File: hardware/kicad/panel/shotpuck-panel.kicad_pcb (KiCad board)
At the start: 2 copper layers, 91 x 88.6 mm, 281 parts, among them J1_0 Samzo PR5L4015-2P-C-F, J1_1 Samzo PR5L4015-2P-C-F, J1_2 Samzo PR5L4015-2P-C-F, J1_3 Samzo PR5L4015-2P-C-F, J2_0 SWD pads, J2_1 SWD pads, J2_2 SWD pads, J2_3 SWD pads, Q1_0 DMN63D8LDW, Q1_1 DMN63D8LDW, Q1_2 DMN63D8LDW, Q1_3 DMN63D8LDW, Q2_0 DMN2004DWK, Q2_1 DMN2004DWK, Q2_2 DMN2004DWK, Q2_3 DMN2004DWK, U1_0 MDBT50Q-1MV2, U1_1 MDBT50Q-1MV2, U1_2 MDBT50Q-1MV2, U1_3 MDBT50Q-1MV2, U2_0 LSM6DSO32TR, U2_1 LSM6DSO32TR, U2_2 LSM6DSO32TR, U2_3 LSM6DSO32TR, U3_0 MCP73831T-2ACI/OT, U3_1 MCP73831T-2ACI/OT, U3_2 MCP73831T-2ACI/OT, U3_3 MCP73831T-2ACI/OT, U4_0 BQ29700DSER, U4_1 BQ29700DSER, U4_2 BQ29700DSER, U4_3 BQ29700DSER

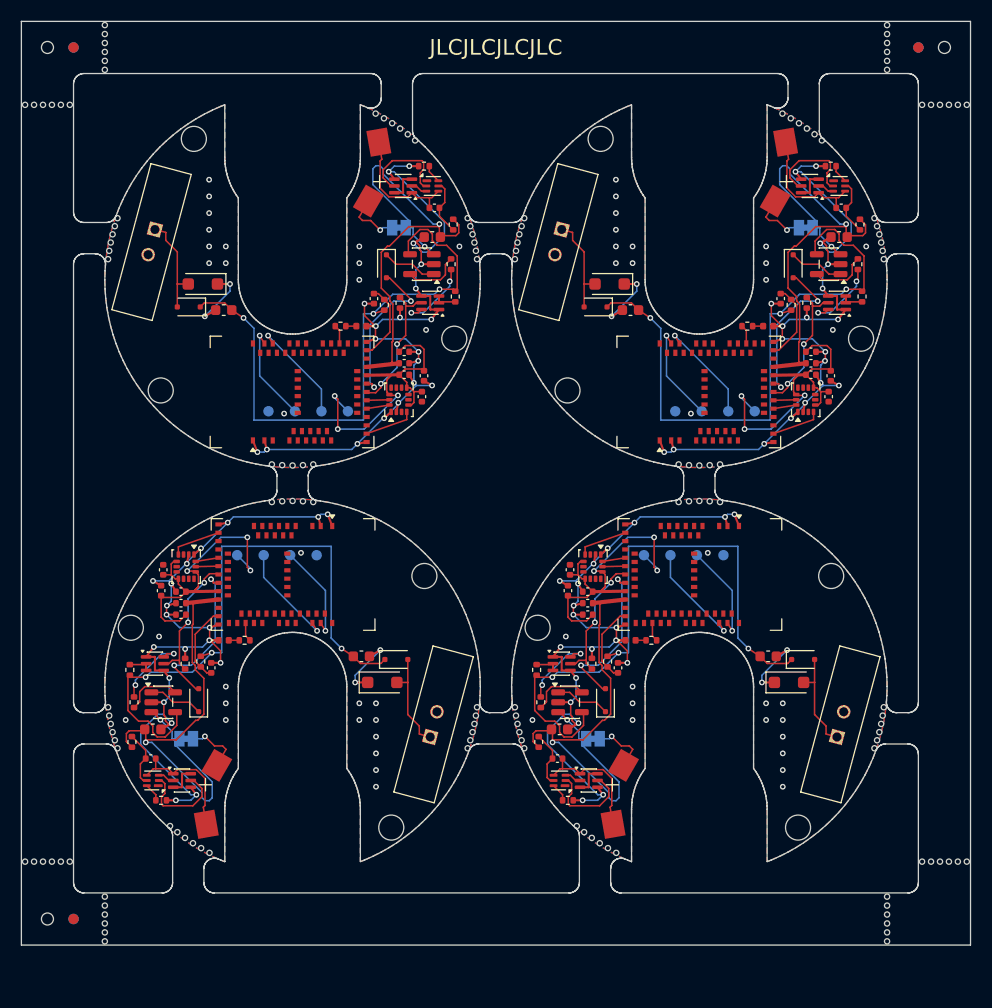
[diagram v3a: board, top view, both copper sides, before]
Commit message: Update ShotPuck design to integrate u-blox BMD-340 module and enhance documentation
- Replaced the Raytac MDBT50Q-1MV2 with the u-blox BMD-340-A-R-10 in the hardware design, updating relevant specifications in `HANDOVER.md`, `README.md`, and `VALIDATION.md`.
- Adjusted pin mappings and configurations in firmware files to reflect the new module's layout and capabilities.
- Enhanced `layout.json` and `design.py` to accommodate the new component dimensions and positions.
- Updated the bill of materials and JLCPCB configurations in `gen_bom.py` and `gen_jlc.py` to ensure accurate sourcing of the new module.
- Revised mechanical design parameters in `board_shape.py` to improve fit and stability.

Co-Authored-By: Claude Opus 5.5 <noreply@anthropic.com>
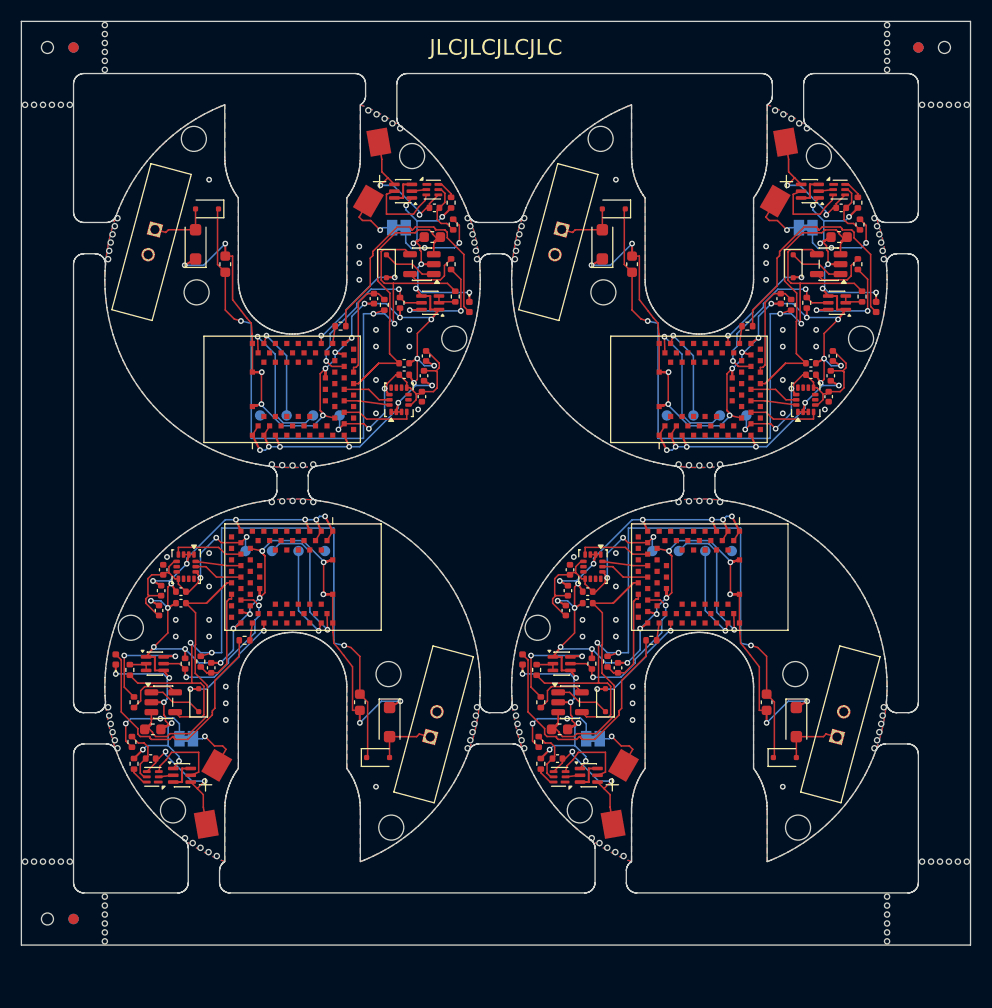
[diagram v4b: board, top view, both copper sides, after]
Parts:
- removed KiKit_MB_12_6, KiKit_MB_13_1, KiKit_MB_16_6, KiKit_MB_1_1, KiKit_MB_4_6, KiKit_MB_5_1, KiKit_MB_8_6, KiKit_MB_9_1: NPTH, NPTH
- added H4_0: M2, ShotPuck:MountingHole_2.4mm_NPTH, F.Cu at (140.5, 32.9)
- added H4_1: M2, ShotPuck:MountingHole_2.4mm_NPTH, F.Cu at (179.5, 32.9)
- added H4_2: M2, ShotPuck:MountingHole_2.4mm_NPTH, F.Cu at (117.5, 95.6)
- added H4_3: M2, ShotPuck:MountingHole_2.4mm_NPTH, F.Cu at (156.5, 95.6)
- added KiKit_MB_10_6: NPTH, NPTH, F.Cu at (145.8, 89.7)
- added KiKit_MB_14_6: NPTH, NPTH, F.Cu at (184.8, 89.7)
- added KiKit_MB_2_6: NPTH, NPTH, F.Cu at (112.2, 38.9)
- added KiKit_MB_6_6: NPTH, NPTH, F.Cu at (151.2, 38.9)
- U1_0, U1_1, U1_2, U1_3: value MDBT50Q-1MV2 -> BMD-340-A-R; footprint RF_Module:Raytac_MDBT50Q -> ShotPuck:u-blox_BMD-340
- moved KiKit_MB_14_1 27.8 mm to (185.7, 85.8)
- moved KiKit_MB_16_1 27.8 mm to (166.0, 66.1)
- moved KiKit_MB_10_1 27.8 mm to (146.7, 85.8)
- moved KiKit_MB_12_1 27.8 mm to (127.0, 66.1)
- moved KiKit_MB_6_1 27.8 mm to (150.3, 42.8)
- moved KiKit_MB_8_1 27.8 mm to (170.0, 62.5)
- moved KiKit_MB_2_1 27.8 mm to (111.3, 42.8)
- moved KiKit_MB_4_1 27.8 mm to (131.0, 62.5)
- moved KiKit_MB_14_2 27.7 mm to (185.6, 86.6)
- moved KiKit_MB_16_2 27.7 mm to (167.0, 66.0)
- moved KiKit_MB_10_2 27.7 mm to (146.6, 86.6)
- moved KiKit_MB_12_2 27.7 mm to (128.0, 66.0)
- moved KiKit_MB_6_2 27.7 mm to (150.4, 42.0)
- moved KiKit_MB_8_2 27.7 mm to (169.0, 62.5)
- moved KiKit_MB_2_2 27.7 mm to (111.4, 42.0)
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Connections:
- Q2_0 pad 1: Board_0-BAT_N -> Board_0-GND
- Q2_0 pad 2: Board_0-PCM_DOUT -> Board_0-PCM_COUT
- Q2_0 pad 4: Board_0-GND -> Board_0-BAT_N
- Q2_0 pad 5: Board_0-PCM_COUT -> Board_0-PCM_DOUT
- Q2_1 pad 1: Board_1-BAT_N -> Board_1-GND
- Q2_1 pad 2: Board_1-PCM_DOUT -> Board_1-PCM_COUT
- Q2_1 pad 4: Board_1-GND -> Board_1-BAT_N
- Q2_1 pad 5: Board_1-PCM_COUT -> Board_1-PCM_DOUT
- Q2_2 pad 1: Board_2-BAT_N -> Board_2-GND
- Q2_2 pad 2: Board_2-PCM_DOUT -> Board_2-PCM_COUT
- Q2_2 pad 4: Board_2-GND -> Board_2-BAT_N
- Q2_2 pad 5: Board_2-PCM_COUT -> Board_2-PCM_DOUT
- Q2_3 pad 1: Board_3-BAT_N -> Board_3-GND
- Q2_3 pad 2: Board_3-PCM_DOUT -> Board_3-PCM_COUT
- Q2_3 pad 4: Board_3-GND -> Board_3-BAT_N
- Q2_3 pad 5: Board_3-PCM_COUT -> Board_3-PCM_DOUT
- U1_0 pad 15: Board_0-GND -> (no net)
- U1_0 pad 16: Board_0-ACC_INT1 -> Board_0-GND
- U1_0 pad 17: (no net) -> Board_0-VDD
- U1_0 pad 18: (no net) -> Board_0-GND
- U1_0 pad 19: (no net) -> Board_0-ACC_INT1
- U1_0 pad 20: Board_0-SDA -> (no net)
- U1_0 pad 21: (no net) -> Board_0-SDA
- U1_0 pad 22: Board_0-SCL -> (no net)
- U1_0 pad 23: (no net) -> Board_0-SCL
- U1_0 pad 24: Board_0-CHG_INH -> (no net)
- U1_0 pad 26: Board_0-CHG_STAT -> (no net)
- U1_0 pad 27: (no net) -> Board_0-CHG_INH
- U1_0 pad 28: Board_0-VDD -> (no net)
- U1_0 pad 29: (no net) -> Board_0-GND
- U1_0 pad 3: (no net) -> Board_0-GND
- U1_0 pad 30: Board_0-VBAT -> Board_0-GND
- U1_0 pad 31: (no net) -> Board_0-LED_IO
- U1_0 pad 32: Board_0-VBUS_SNS -> (no net)
- U1_0 pad 33: Board_0-GND -> Board_0-CHG_STAT
- U1_0 pad 37: Board_0-LED_IO -> (no net)
- U1_0 pad 4: (no net) -> Board_0-GND
- U1_0 pad 43: (no net) -> Board_0-SWDCLK
- U1_0 pad 44: (no net) -> Board_0-SWDIO
- U1_0 pad 45: (no net) -> Board_0-GND
- U1_0 pad 46: (no net) -> Board_0-GND
- U1_0 pad 47: (no net) -> Board_0-GND
- U1_0 pad 5: (no net) -> Board_0-GND
- U1_0 pad 51: Board_0-SWDIO -> (no net)
- U1_0 pad 53: Board_0-SWDCLK -> (no net)
- U1_1 pad 15: Board_1-GND -> (no net)
- U1_1 pad 16: Board_1-ACC_INT1 -> Board_1-GND
- U1_1 pad 17: (no net) -> Board_1-VDD
- U1_1 pad 18: (no net) -> Board_1-GND
- U1_1 pad 19: (no net) -> Board_1-ACC_INT1
- U1_1 pad 20: Board_1-SDA -> (no net)
- U1_1 pad 21: (no net) -> Board_1-SDA
- U1_1 pad 22: Board_1-SCL -> (no net)
- U1_1 pad 23: (no net) -> Board_1-SCL
- U1_1 pad 24: Board_1-CHG_INH -> (no net)
- U1_1 pad 26: Board_1-CHG_STAT -> (no net)
- U1_1 pad 27: (no net) -> Board_1-CHG_INH
- U1_1 pad 28: Board_1-VDD -> (no net)
- U1_1 pad 29: (no net) -> Board_1-GND
- U1_1 pad 3: (no net) -> Board_1-GND
- U1_1 pad 30: Board_1-VBAT -> Board_1-GND
- U1_1 pad 31: (no net) -> Board_1-LED_IO
- U1_1 pad 32: Board_1-VBUS_SNS -> (no net)
- U1_1 pad 33: Board_1-GND -> Board_1-CHG_STAT
- U1_1 pad 37: Board_1-LED_IO -> (no net)
- U1_1 pad 4: (no net) -> Board_1-GND
- U1_1 pad 43: (no net) -> Board_1-SWDCLK
- U1_1 pad 44: (no net) -> Board_1-SWDIO
- U1_1 pad 45: (no net) -> Board_1-GND
- U1_1 pad 46: (no net) -> Board_1-GND
- U1_1 pad 47: (no net) -> Board_1-GND
- U1_1 pad 5: (no net) -> Board_1-GND
- U1_1 pad 51: Board_1-SWDIO -> (no net)
- U1_1 pad 53: Board_1-SWDCLK -> (no net)
- U1_2 pad 15: Board_2-GND -> (no net)
- U1_2 pad 16: Board_2-ACC_INT1 -> Board_2-GND
- U1_2 pad 17: (no net) -> Board_2-VDD
- U1_2 pad 18: (no net) -> Board_2-GND
- U1_2 pad 19: (no net) -> Board_2-ACC_INT1
- U1_2 pad 20: Board_2-SDA -> (no net)
- U1_2 pad 21: (no net) -> Board_2-SDA
- U1_2 pad 22: Board_2-SCL -> (no net)
- U1_2 pad 23: (no net) -> Board_2-SCL
- U1_2 pad 24: Board_2-CHG_INH -> (no net)
- U1_2 pad 26: Board_2-CHG_STAT -> (no net)
- U1_2 pad 27: (no net) -> Board_2-CHG_INH
- U1_2 pad 28: Board_2-VDD -> (no net)
- U1_2 pad 29: (no net) -> Board_2-GND
- U1_2 pad 3: (no net) -> Board_2-GND
- U1_2 pad 30: Board_2-VBAT -> Board_2-GND
- U1_2 pad 31: (no net) -> Board_2-LED_IO
- U1_2 pad 32: Board_2-VBUS_SNS -> (no net)
- U1_2 pad 33: Board_2-GND -> Board_2-CHG_STAT
- U1_2 pad 37: Board_2-LED_IO -> (no net)
- U1_2 pad 4: (no net) -> Board_2-GND
- U1_2 pad 43: (no net) -> Board_2-SWDCLK
- U1_2 pad 44: (no net) -> Board_2-SWDIO
- U1_2 pad 45: (no net) -> Board_2-GND
- U1_2 pad 46: (no net) -> Board_2-GND
- U1_2 pad 47: (no net) -> Board_2-GND
- U1_2 pad 5: (no net) -> Board_2-GND
- U1_2 pad 51: Board_2-SWDIO -> (no net)
- U1_2 pad 53: Board_2-SWDCLK -> (no net)
- U1_3 pad 15: Board_3-GND -> (no net)
- U1_3 pad 16: Board_3-ACC_INT1 -> Board_3-GND
- U1_3 pad 17: (no net) -> Board_3-VDD
- U1_3 pad 18: (no net) -> Board_3-GND
- U1_3 pad 19: (no net) -> Board_3-ACC_INT1
- U1_3 pad 20: Board_3-SDA -> (no net)
- U1_3 pad 21: (no net) -> Board_3-SDA
- U1_3 pad 22: Board_3-SCL -> (no net)
- U1_3 pad 23: (no net) -> Board_3-SCL
- U1_3 pad 24: Board_3-CHG_INH -> (no net)
- U1_3 pad 26: Board_3-CHG_STAT -> (no net)
- U1_3 pad 27: (no net) -> Board_3-CHG_INH
- U1_3 pad 28: Board_3-VDD -> (no net)
- U1_3 pad 29: (no net) -> Board_3-GND
- U1_3 pad 3: (no net) -> Board_3-GND
- U1_3 pad 30: Board_3-VBAT -> Board_3-GND
- U1_3 pad 31: (no net) -> Board_3-LED_IO
- U1_3 pad 32: Board_3-VBUS_SNS -> (no net)
- U1_3 pad 33: Board_3-GND -> Board_3-CHG_STAT
- U1_3 pad 37: Board_3-LED_IO -> (no net)
- U1_3 pad 4: (no net) -> Board_3-GND
- U1_3 pad 43: (no net) -> Board_3-SWDCLK
- U1_3 pad 44: (no net) -> Board_3-SWDIO
- U1_3 pad 45: (no net) -> Board_3-GND
- U1_3 pad 46: (no net) -> Board_3-GND
- U1_3 pad 47: (no net) -> Board_3-GND
- U1_3 pad 5: (no net) -> Board_3-GND
- U1_3 pad 51: Board_3-SWDIO -> (no net)
- U1_3 pad 53: Board_3-SWDCLK -> (no net)
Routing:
- net Board_3-GND: track 86.8 -> 131.6 mm, vias 35 -> 37
- net Board_2-GND: track 86.8 -> 131.6 mm, vias 35 -> 37
- net Board_1-GND: track 86.8 -> 131.6 mm, vias 35 -> 37
- net Board_0-GND: track 86.8 -> 131.6 mm, vias 35 -> 37
- net Board_2-LED_A: track 1.00 -> 25.4 mm
- net Board_3-LED_A: track 1.00 -> 25.4 mm
- net Board_1-LED_A: track 1.00 -> 25.4 mm
- net Board_0-LED_A: track 1.00 -> 25.4 mm
- net Board_0-VIN: track 58.1 -> 68.4 mm
- net Board_3-VIN: track 58.1 -> 68.4 mm
- net Board_1-VIN: track 58.1 -> 68.4 mm
- net Board_2-VIN: track 58.1 -> 68.4 mm
- net Board_2-PCM_COUT: track 9.30 -> 1.40 mm
- net Board_3-PCM_COUT: track 9.30 -> 1.40 mm
- net Board_1-PCM_COUT: track 9.30 -> 1.40 mm
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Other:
- outline, holes or cut-outs redrawn

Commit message: Switch J1 to waterproof IPX8 USB-C (C3020041) and seal the cap
- J1: SHOU HAN TYPE-C 6PFS 2JCB1.6-H6.7 IPX8 (LCSC C3020041), recessed
  into a 10.28 x 5.22 mm notch in the board edge at 132.58 deg, midway
  between H1 and H2. Footprint from the datasheet drawing (pads kept
  0.3/0.35 mm from the notch; the notch sides run through two 0.70 mm
  NPTH holes for the legs, since the datasheet's 0.69 mm U-slots cannot
  be routed); LCSC's STEP model shifted -1.93 mm onto the pads.
- H1/H2 moved apart so the ground pour reaches the wing tabs; layout.json
  bosses follow (plate holes, cap bosses, standoffs).
- GND via at (-0.41, 16.09): the pour around U2's GND pins 6/7 reached
  the rest of GND only along the rim, where the top tab's mouse bites cut
  it.
- Cap: the silicone ring seals in an obround hole in the wall (0.15 mm
  squeeze per side), a flat at the receptacle face lets any compliant
  plug seat fully, a pocket over the body leaves 0.67 mm of cap top.
  CadQuery check with the real STEP model: only the ring squeeze
  overlaps; a maximum-size plug overmold clears cap and plate.
- Panel: 2 mm backbone between the rows, top tab 1.5 mm wide at 86 deg
  (clear of H1 and the via at 80 deg); panel 91.1 x 92.7 mm.
- gen_panel.py places tabs from the board's own centre (the board sits at
  (132.06, 91.40) on the KiCad page); the Blender GLB export uses the
  same origin and takes J1 from the board.
- Board DRC 0/0 with schematic parity; panel DRC 0/0; BOM/CPL/Gerbers
  regenerated.

mechanical/out/shotpuck_assembly.mp4 and .blend are from the render
before the waterproof port and still show the earlier cap; re-render
with mechanical/blender/render_assembly.py. gen_pcb.py does not draw
the port notch, and design.py still lists C5.

Co-Authored-By: Claude Opus 5.5 <noreply@anthropic.com>
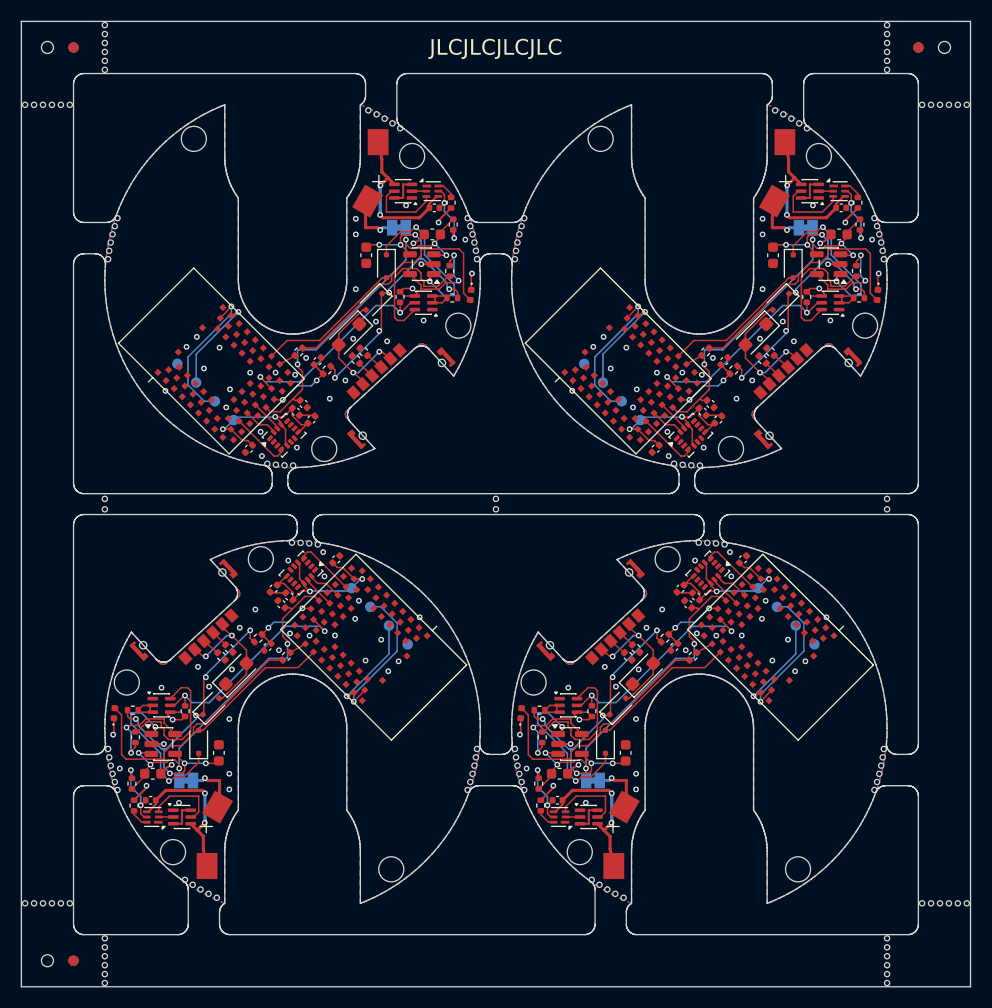
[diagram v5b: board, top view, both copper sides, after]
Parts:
- removed C5_0, C5_1, C5_2, C5_3: 100n, Capacitor_SMD:C_0402_1005Metric
- removed KiKit_MB_10_5, KiKit_MB_10_6, KiKit_MB_11_1, KiKit_MB_14_5, KiKit_MB_14_6, KiKit_MB_15_1, KiKit_MB_17_4, KiKit_MB_17_5, KiKit_MB_17_6, KiKit_MB_17_7, KiKit_MB_18_4, KiKit_MB_18_5, KiKit_MB_18_6, KiKit_MB_18_7, KiKit_MB_19_4, KiKit_MB_19_5, KiKit_MB_19_6, KiKit_MB_19_7, KiKit_MB_2_5, KiKit_MB_2_6, KiKit_MB_3_1, KiKit_MB_6_5, KiKit_MB_6_6, KiKit_MB_7_1: NPTH, NPTH
- added KiKit_MB_12_6: NPTH, NPTH, F.Cu at (111.3, 89.8)
- added KiKit_MB_13_1: NPTH, NPTH, F.Cu at (185.7, 89.8)
- added KiKit_MB_16_6: NPTH, NPTH, F.Cu at (150.3, 89.8)
- added KiKit_MB_1_1: NPTH, NPTH, F.Cu at (111.3, 42.8)
- added KiKit_MB_25_2: NPTH, NPTH, F.Cu at (103.4, 104.6)
- added KiKit_MB_25_3: NPTH, NPTH, F.Cu at (104.2, 104.6)
- added KiKit_MB_25_4: NPTH, NPTH, F.Cu at (105.1, 104.6)
- added KiKit_MB_25_5: NPTH, NPTH, F.Cu at (105.9, 104.6)
- added KiKit_MB_25_6: NPTH, NPTH, F.Cu at (106.8, 104.6)
- added KiKit_MB_25_7: NPTH, NPTH, F.Cu at (107.6, 104.6)
- added KiKit_MB_26_2: NPTH, NPTH, F.Cu at (189.4, 28.0)
- added KiKit_MB_26_3: NPTH, NPTH, F.Cu at (190.2, 28.0)
- added KiKit_MB_26_4: NPTH, NPTH, F.Cu at (191.1, 28.0)
- added KiKit_MB_26_5: NPTH, NPTH, F.Cu at (191.9, 28.0)
- added KiKit_MB_26_6: NPTH, NPTH, F.Cu at (192.8, 28.0)
- added KiKit_MB_26_7: NPTH, NPTH, F.Cu at (193.6, 28.0)
- added KiKit_MB_27_2: NPTH, NPTH, F.Cu at (189.4, 104.6)
- added KiKit_MB_27_3: NPTH, NPTH, F.Cu at (190.2, 104.6)
- added KiKit_MB_27_4: NPTH, NPTH, F.Cu at (191.1, 104.6)
- added KiKit_MB_27_5: NPTH, NPTH, F.Cu at (191.9, 104.6)
- added KiKit_MB_27_6: NPTH, NPTH, F.Cu at (192.8, 104.6)
- added KiKit_MB_27_7: NPTH, NPTH, F.Cu at (193.6, 104.6)
- added KiKit_MB_4_6: NPTH, NPTH, F.Cu at (146.7, 42.8)
- added KiKit_MB_5_1: NPTH, NPTH, F.Cu at (150.3, 42.8)
- added KiKit_MB_8_6: NPTH, NPTH, F.Cu at (185.7, 42.8)
- added KiKit_MB_9_1: NPTH, NPTH, F.Cu at (146.7, 89.8)
- added R10_0: 5.1k 1%, Resistor_SMD:R_0402_1005Metric, F.Cu at (135.1, 52.4)
- added R10_1: 5.1k 1%, Resistor_SMD:R_0402_1005Metric, F.Cu at (174.1, 52.4)
- added R10_2: 5.1k 1%, Resistor_SMD:R_0402_1005Metric, F.Cu at (122.9, 80.1)
- added R10_3: 5.1k 1%, Resistor_SMD:R_0402_1005Metric, F.Cu at (161.9, 80.1)
- added R11_0: 5.1k 1%, Resistor_SMD:R_0402_1005Metric, F.Cu at (135.8, 51.7)
- added R11_1: 5.1k 1%, Resistor_SMD:R_0402_1005Metric, F.Cu at (174.8, 51.7)
- added R11_2: 5.1k 1%, Resistor_SMD:R_0402_1005Metric, F.Cu at (122.2, 80.9)
- added R11_3: 5.1k 1%, Resistor_SMD:R_0402_1005Metric, F.Cu at (161.2, 80.9)
- BT1_0, BT1_1, BT1_2, BT1_3: footprint ShotPuck:LIR1254_Contacts -> ShotPuck:LIR1254_Contacts_Edit
- J1_0, J1_1, J1_2, J1_3: value Samzo PR5L4015-2P-C-F -> TYPE-C 6PFS 2JCB1.6-H6.7 IPX8; footprint ShotPuck:MagPogo_Samzo_2P -> ShotPuck:USB_C_Receptacle_ShouHan_TYPE-C-6PFS-2JCB1.6-H6.7_IPX8
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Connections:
- net Board_0-ACC_INT1 renamed Board_0-/ACC_INT1
- net Board_0-BAT_N renamed Board_0-/BAT_N
- net Board_0-BAT_P renamed Board_0-/BAT_P
- net Board_0-CHG_INH renamed Board_0-/CHG_INH
- net Board_0-CHG_STAT renamed Board_0-/CHG_STAT
- net Board_0-LED_A renamed Board_0-/LED_A
- net Board_0-LED_IO renamed Board_0-/LED_IO
- net Board_0-PCM_BAT renamed Board_0-/PCM_BAT
- net Board_0-PCM_COUT renamed Board_0-/PCM_COUT
- net Board_0-PCM_D renamed Board_0-/PCM_D
- net Board_0-PCM_DOUT renamed Board_0-/PCM_DOUT
- net Board_0-PCM_VM renamed Board_0-/PCM_VM
- net Board_0-PROG renamed Board_0-/PROG
- net Board_0-PROG_SW renamed Board_0-/PROG_SW
- net Board_0-Q1_GATE renamed Board_0-/Q1_GATE
- net Board_0-SCL renamed Board_0-/SCL
- net Board_0-SDA renamed Board_0-/SDA
- net Board_0-STAT renamed Board_0-/STAT
- net Board_0-SWDCLK renamed Board_0-/SWDCLK
- net Board_0-SWDIO renamed Board_0-/SWDIO
- net Board_0-VBAT renamed Board_0-/VBAT
- net Board_0-VBUS_SNS renamed Board_0-/VBUS_SNS
- net Board_0-VDD renamed Board_0-/VDD
- net Board_0-VIN renamed Board_0-/VIN
- net Board_1-ACC_INT1 renamed Board_1-/ACC_INT1
- net Board_1-BAT_N renamed Board_1-/BAT_N
- net Board_1-BAT_P renamed Board_1-/BAT_P
- net Board_1-CHG_INH renamed Board_1-/CHG_INH
- net Board_1-CHG_STAT renamed Board_1-/CHG_STAT
- net Board_1-LED_A renamed Board_1-/LED_A
- net Board_1-LED_IO renamed Board_1-/LED_IO
- net Board_1-PCM_BAT renamed Board_1-/PCM_BAT
- net Board_1-PCM_COUT renamed Board_1-/PCM_COUT
- net Board_1-PCM_D renamed Board_1-/PCM_D
- net Board_1-PCM_DOUT renamed Board_1-/PCM_DOUT
- net Board_1-PCM_VM renamed Board_1-/PCM_VM
- net Board_1-PROG renamed Board_1-/PROG
- net Board_1-PROG_SW renamed Board_1-/PROG_SW
- net Board_1-Q1_GATE renamed Board_1-/Q1_GATE
- net Board_1-SCL renamed Board_1-/SCL
- net Board_1-SDA renamed Board_1-/SDA
- net Board_1-STAT renamed Board_1-/STAT
- net Board_1-SWDCLK renamed Board_1-/SWDCLK
- net Board_1-SWDIO renamed Board_1-/SWDIO
- net Board_1-VBAT renamed Board_1-/VBAT
- net Board_1-VBUS_SNS renamed Board_1-/VBUS_SNS
- net Board_1-VDD renamed Board_1-/VDD
- net Board_1-VIN renamed Board_1-/VIN
- net Board_2-ACC_INT1 renamed Board_2-/ACC_INT1
- net Board_2-BAT_N renamed Board_2-/BAT_N
- net Board_2-BAT_P renamed Board_2-/BAT_P
- net Board_2-CHG_INH renamed Board_2-/CHG_INH
- net Board_2-CHG_STAT renamed Board_2-/CHG_STAT
- net Board_2-LED_A renamed Board_2-/LED_A
- net Board_2-LED_IO renamed Board_2-/LED_IO
- net Board_2-PCM_BAT renamed Board_2-/PCM_BAT
- net Board_2-PCM_COUT renamed Board_2-/PCM_COUT
- net Board_2-PCM_D renamed Board_2-/PCM_D
- net Board_2-PCM_DOUT renamed Board_2-/PCM_DOUT
- net Board_2-PCM_VM renamed Board_2-/PCM_VM
- net Board_2-PROG renamed Board_2-/PROG
- net Board_2-PROG_SW renamed Board_2-/PROG_SW
- net Board_2-Q1_GATE renamed Board_2-/Q1_GATE
- net Board_2-SCL renamed Board_2-/SCL
- net Board_2-SDA renamed Board_2-/SDA
- net Board_2-STAT renamed Board_2-/STAT
- net Board_2-SWDCLK renamed Board_2-/SWDCLK
- net Board_2-SWDIO renamed Board_2-/SWDIO
- net Board_2-VBAT renamed Board_2-/VBAT
- net Board_2-VBUS_SNS renamed Board_2-/VBUS_SNS
- net Board_2-VDD renamed Board_2-/VDD
- net Board_2-VIN renamed Board_2-/VIN
- net Board_3-ACC_INT1 renamed Board_3-/ACC_INT1
- net Board_3-BAT_N renamed Board_3-/BAT_N
- net Board_3-BAT_P renamed Board_3-/BAT_P
- net Board_3-CHG_INH renamed Board_3-/CHG_INH
- net Board_3-CHG_STAT renamed Board_3-/CHG_STAT
- net Board_3-LED_A renamed Board_3-/LED_A
- net Board_3-LED_IO renamed Board_3-/LED_IO
- net Board_3-PCM_BAT renamed Board_3-/PCM_BAT
- net Board_3-PCM_COUT renamed Board_3-/PCM_COUT
- net Board_3-PCM_D renamed Board_3-/PCM_D
- net Board_3-PCM_DOUT renamed Board_3-/PCM_DOUT
- net Board_3-PCM_VM renamed Board_3-/PCM_VM
- net Board_3-PROG renamed Board_3-/PROG
- net Board_3-PROG_SW renamed Board_3-/PROG_SW
- net Board_3-Q1_GATE renamed Board_3-/Q1_GATE
- net Board_3-SCL renamed Board_3-/SCL
- net Board_3-SDA renamed Board_3-/SDA
- net Board_3-STAT renamed Board_3-/STAT
- net Board_3-SWDCLK renamed Board_3-/SWDCLK
- net Board_3-SWDIO renamed Board_3-/SWDIO
- net Board_3-VBAT renamed Board_3-/VBAT
- net Board_3-VBUS_SNS renamed Board_3-/VBUS_SNS
- net Board_3-VDD renamed Board_3-/VDD
- net Board_3-VIN renamed Board_3-/VIN
- C1_0 pad 2: Board_0-GND -> Board_0-/GND
- C1_1 pad 2: Board_1-GND -> Board_1-/GND
- C1_2 pad 2: Board_2-GND -> Board_2-/GND
- C1_3 pad 2: Board_3-GND -> Board_3-/GND
- C2_0 pad 2: Board_0-GND -> Board_0-/GND
- C2_1 pad 2: Board_1-GND -> Board_1-/GND
- C2_2 pad 2: Board_2-GND -> Board_2-/GND
- C2_3 pad 2: Board_3-GND -> Board_3-/GND
- C3_0 pad 2: Board_0-GND -> Board_0-/GND
- C3_1 pad 2: Board_1-GND -> Board_1-/GND
- C3_2 pad 2: Board_2-GND -> Board_2-/GND
- C3_3 pad 2: Board_3-GND -> Board_3-/GND
- C4_0 pad 2: Board_0-GND -> Board_0-/GND
- C4_1 pad 2: Board_1-GND -> Board_1-/GND
- C4_2 pad 2: Board_2-GND -> Board_2-/GND
- C4_3 pad 2: Board_3-GND -> Board_3-/GND
- C6_0 pad 2: Board_0-GND -> Board_0-/GND
- C6_1 pad 2: Board_1-GND -> Board_1-/GND
- C6_2 pad 2: Board_2-GND -> Board_2-/GND
- C6_3 pad 2: Board_3-GND -> Board_3-/GND
- C7_0 pad 2: Board_0-GND -> Board_0-/GND
- C7_1 pad 2: Board_1-GND -> Board_1-/GND
- C7_2 pad 2: Board_2-GND -> Board_2-/GND
- C7_3 pad 2: Board_3-GND -> Board_3-/GND
- C9_0 pad 2: Board_0-GND -> Board_0-/GND
- C9_1 pad 2: Board_1-GND -> Board_1-/GND
- C9_2 pad 2: Board_2-GND -> Board_2-/GND
- C9_3 pad 2: Board_3-GND -> Board_3-/GND
- D1_0 pad 2: Board_0-VIN_RAW -> Board_0-/VIN_RAW
- D1_1 pad 2: Board_1-VIN_RAW -> Board_1-/VIN_RAW
- D1_2 pad 2: Board_2-VIN_RAW -> Board_2-/VIN_RAW
- D1_3 pad 2: Board_3-VIN_RAW -> Board_3-/VIN_RAW
- D3_0 pad 1: Board_0-GND -> Board_0-/GND
- D3_0 pad 2: Board_0-VIN_RAW -> Board_0-/VIN_RAW
- D3_1 pad 1: Board_1-GND -> Board_1-/GND
- D3_1 pad 2: Board_1-VIN_RAW -> Board_1-/VIN_RAW
- D3_2 pad 1: Board_2-GND -> Board_2-/GND
- D3_2 pad 2: Board_2-VIN_RAW -> Board_2-/VIN_RAW
- D3_3 pad 1: Board_3-GND -> Board_3-/GND
- D3_3 pad 2: Board_3-VIN_RAW -> Board_3-/VIN_RAW
- D4_0 pad 1: Board_0-GND -> Board_0-/GND
- D4_1 pad 1: Board_1-GND -> Board_1-/GND
- D4_2 pad 1: Board_2-GND -> Board_2-/GND
- D4_3 pad 1: Board_3-GND -> Board_3-/GND
- J2_0 pad 4: Board_0-GND -> Board_0-/GND
- J2_1 pad 4: Board_1-GND -> Board_1-/GND
- J2_2 pad 4: Board_2-GND -> Board_2-/GND
- J2_3 pad 4: Board_3-GND -> Board_3-/GND
- Q1_0 pad 1: Board_0-GND -> Board_0-/GND
- Q1_0 pad 4: Board_0-GND -> Board_0-/GND
- Q1_1 pad 1: Board_1-GND -> Board_1-/GND
- Q1_1 pad 4: Board_1-GND -> Board_1-/GND
- Q1_2 pad 1: Board_2-GND -> Board_2-/GND
- Q1_2 pad 4: Board_2-GND -> Board_2-/GND
- Q1_3 pad 1: Board_3-GND -> Board_3-/GND
- Q1_3 pad 4: Board_3-GND -> Board_3-/GND
- Q2_0 pad 1: Board_0-GND -> Board_0-/GND
- Q2_1 pad 1: Board_1-GND -> Board_1-/GND
- Q2_2 pad 1: Board_2-GND -> Board_2-/GND
- Q2_3 pad 1: Board_3-GND -> Board_3-/GND
- R3_0 pad 2: Board_0-GND -> Board_0-/GND
- R3_1 pad 2: Board_1-GND -> Board_1-/GND
- R3_2 pad 2: Board_2-GND -> Board_2-/GND
- R3_3 pad 2: Board_3-GND -> Board_3-/GND
- R8_0 pad 2: Board_0-GND -> Board_0-/GND
- R8_1 pad 2: Board_1-GND -> Board_1-/GND
- R8_2 pad 2: Board_2-GND -> Board_2-/GND
- R8_3 pad 2: Board_3-GND -> Board_3-/GND
- U1_0 pad 1: Board_0-GND -> Board_0-/GND
- U1_0 pad 10: (no net) -> Board_0-unconnected-(U1-P0.29-Pad10)
- U1_0 pad 11: (no net) -> Board_0-unconnected-(U1-P0.30-Pad11)
- U1_0 pad 12: (no net) -> Board_0-unconnected-(U1-P0.31-Pad12)
- U1_0 pad 13: (no net) -> Board_0-unconnected-(U1-P0.00-Pad13)
- U1_0 pad 14: (no net) -> Board_0-unconnected-(U1-P0.01-Pad14)
- U1_0 pad 15: (no net) -> Board_0-unconnected-(U1-P0.02-Pad15)
- U1_0 pad 16: Board_0-GND -> Board_0-/GND
- U1_0 pad 18: Board_0-GND -> Board_0-/GND
- U1_0 pad 2: Board_0-GND -> Board_0-/GND
- U1_0 pad 20: (no net) -> Board_0-unconnected-(U1-P0.04-Pad20)
- U1_0 pad 22: (no net) -> Board_0-unconnected-(U1-P0.06-Pad22)
- U1_0 pad 24: (no net) -> Board_0-unconnected-(U1-P0.08-Pad24)
- U1_0 pad 25: (no net) -> Board_0-unconnected-(U1-P0.09-Pad25)
- U1_0 pad 26: (no net) -> Board_0-unconnected-(U1-P0.10-Pad26)
- U1_0 pad 28: (no net) -> Board_0-unconnected-(U1-P0.12-Pad28)
- U1_0 pad 29: Board_0-GND -> Board_0-/GND
- U1_0 pad 3: Board_0-GND -> Board_0-/GND
- U1_0 pad 30: Board_0-GND -> Board_0-/GND
- U1_0 pad 32: (no net) -> Board_0-unconnected-(U1-P0.14-Pad32)
- U1_0 pad 34: (no net) -> Board_0-unconnected-(U1-P0.16-Pad34)
- U1_0 pad 35: (no net) -> Board_0-unconnected-(U1-P0.17-Pad35)
- U1_0 pad 36: (no net) -> Board_0-unconnected-(U1-P0.21-Pad36)
- U1_0 pad 37: (no net) -> Board_0-unconnected-(U1-P0.19-Pad37)
- U1_0 pad 38: (no net) -> Board_0-unconnected-(U1-P0.20-Pad38)
- U1_0 pad 39: (no net) -> Board_0-unconnected-(U1-P0.18-Pad39)
- U1_0 pad 4: Board_0-GND -> Board_0-/GND
- U1_0 pad 40: (no net) -> Board_0-unconnected-(U1-P0.22-Pad40)
- U1_0 pad 41: (no net) -> Board_0-unconnected-(U1-P0.23-Pad41)
- U1_0 pad 42: (no net) -> Board_0-unconnected-(U1-P0.24-Pad42)
- U1_0 pad 45: Board_0-GND -> Board_0-/GND
- U1_0 pad 46: Board_0-GND -> Board_0-/GND
- U1_0 pad 47: Board_0-GND -> Board_0-/GND
- U1_0 pad 48: (no net) -> Board_0-unconnected-(U1-P1.05-Pad48)
- U1_0 pad 49: (no net) -> Board_0-unconnected-(U1-P1.06-Pad49)
- U1_0 pad 5: Board_0-GND -> Board_0-/GND
- U1_0 pad 50: (no net) -> Board_0-unconnected-(U1-P1.07-Pad50)
- U1_0 pad 51: (no net) -> Board_0-unconnected-(U1-P1.08-Pad51)
- U1_0 pad 52: (no net) -> Board_0-unconnected-(U1-P1.09-Pad52)
- U1_0 pad 53: (no net) -> Board_0-unconnected-(U1-P1.10-Pad53)
- U1_0 pad 54: (no net) -> Board_0-unconnected-(U1-P1.11-Pad54)
- U1_0 pad 55: Board_0-GND -> Board_0-/GND
- U1_0 pad 56: (no net) -> Board_0-unconnected-(U1-P1.00-Pad56)
- U1_0 pad 57: (no net) -> Board_0-unconnected-(U1-P1.01-Pad57)
- U1_0 pad 58: (no net) -> Board_0-unconnected-(U1-P1.02-Pad58)
- U1_0 pad 59: (no net) -> Board_0-unconnected-(U1-P1.03-Pad59)
- U1_0 pad 6: (no net) -> Board_0-unconnected-(U1-P0.25-Pad6)
- U1_0 pad 60: (no net) -> Board_0-unconnected-(U1-P1.04-Pad60)
- U1_0 pad 61: (no net) -> Board_0-unconnected-(U1-P1.12-Pad61)
- U1_0 pad 62: (no net) -> Board_0-unconnected-(U1-P1.13-Pad62)
- U1_0 pad 63: (no net) -> Board_0-unconnected-(U1-P1.14-Pad63)
- U1_0 pad 64: (no net) -> Board_0-unconnected-(U1-P1.15-Pad64)
- U1_0 pad 67: (no net) -> Board_0-unconnected-(U1-USB-D--Pad67)
- U1_0 pad 68: (no net) -> Board_0-unconnected-(U1-USB-D+-Pad68)
- U1_0 pad 7: (no net) -> Board_0-unconnected-(U1-P0.26-Pad7)
- U1_0 pad 8: (no net) -> Board_0-unconnected-(U1-P0.27-Pad8)
- U1_0 pad 9: (no net) -> Board_0-unconnected-(U1-P0.28-Pad9)
- U1_1 pad 1: Board_1-GND -> Board_1-/GND
- U1_1 pad 10: (no net) -> Board_1-unconnected-(U1-P0.29-Pad10)
- U1_1 pad 11: (no net) -> Board_1-unconnected-(U1-P0.30-Pad11)
- U1_1 pad 12: (no net) -> Board_1-unconnected-(U1-P0.31-Pad12)
- U1_1 pad 13: (no net) -> Board_1-unconnected-(U1-P0.00-Pad13)
- U1_1 pad 14: (no net) -> Board_1-unconnected-(U1-P0.01-Pad14)
- U1_1 pad 15: (no net) -> Board_1-unconnected-(U1-P0.02-Pad15)
- U1_1 pad 16: Board_1-GND -> Board_1-/GND
- U1_1 pad 18: Board_1-GND -> Board_1-/GND
- U1_1 pad 2: Board_1-GND -> Board_1-/GND
- U1_1 pad 20: (no net) -> Board_1-unconnected-(U1-P0.04-Pad20)
- U1_1 pad 22: (no net) -> Board_1-unconnected-(U1-P0.06-Pad22)
- U1_1 pad 24: (no net) -> Board_1-unconnected-(U1-P0.08-Pad24)
- U1_1 pad 25: (no net) -> Board_1-unconnected-(U1-P0.09-Pad25)
- U1_1 pad 26: (no net) -> Board_1-unconnected-(U1-P0.10-Pad26)
- U1_1 pad 28: (no net) -> Board_1-unconnected-(U1-P0.12-Pad28)
- U1_1 pad 29: Board_1-GND -> Board_1-/GND
- U1_1 pad 3: Board_1-GND -> Board_1-/GND
- U1_1 pad 30: Board_1-GND -> Board_1-/GND
- U1_1 pad 32: (no net) -> Board_1-unconnected-(U1-P0.14-Pad32)
- U1_1 pad 34: (no net) -> Board_1-unconnected-(U1-P0.16-Pad34)
- U1_1 pad 35: (no net) -> Board_1-unconnected-(U1-P0.17-Pad35)
- U1_1 pad 36: (no net) -> Board_1-unconnected-(U1-P0.21-Pad36)
- U1_1 pad 37: (no net) -> Board_1-unconnected-(U1-P0.19-Pad37)
- U1_1 pad 38: (no net) -> Board_1-unconnected-(U1-P0.20-Pad38)
- U1_1 pad 39: (no net) -> Board_1-unconnected-(U1-P0.18-Pad39)
- U1_1 pad 4: Board_1-GND -> Board_1-/GND
- U1_1 pad 40: (no net) -> Board_1-unconnected-(U1-P0.22-Pad40)
- U1_1 pad 41: (no net) -> Board_1-unconnected-(U1-P0.23-Pad41)
- U1_1 pad 42: (no net) -> Board_1-unconnected-(U1-P0.24-Pad42)
- U1_1 pad 45: Board_1-GND -> Board_1-/GND
- U1_1 pad 46: Board_1-GND -> Board_1-/GND
- U1_1 pad 47: Board_1-GND -> Board_1-/GND
- U1_1 pad 48: (no net) -> Board_1-unconnected-(U1-P1.05-Pad48)
- U1_1 pad 49: (no net) -> Board_1-unconnected-(U1-P1.06-Pad49)
- U1_1 pad 5: Board_1-GND -> Board_1-/GND
- U1_1 pad 50: (no net) -> Board_1-unconnected-(U1-P1.07-Pad50)
- U1_1 pad 51: (no net) -> Board_1-unconnected-(U1-P1.08-Pad51)
- U1_1 pad 52: (no net) -> Board_1-unconnected-(U1-P1.09-Pad52)
- U1_1 pad 53: (no net) -> Board_1-unconnected-(U1-P1.10-Pad53)
- U1_1 pad 54: (no net) -> Board_1-unconnected-(U1-P1.11-Pad54)
- U1_1 pad 55: Board_1-GND -> Board_1-/GND
- U1_1 pad 56: (no net) -> Board_1-unconnected-(U1-P1.00-Pad56)
- U1_1 pad 57: (no net) -> Board_1-unconnected-(U1-P1.01-Pad57)
- U1_1 pad 58: (no net) -> Board_1-unconnected-(U1-P1.02-Pad58)
- U1_1 pad 59: (no net) -> Board_1-unconnected-(U1-P1.03-Pad59)
- U1_1 pad 6: (no net) -> Board_1-unconnected-(U1-P0.25-Pad6)
- U1_1 pad 60: (no net) -> Board_1-unconnected-(U1-P1.04-Pad60)
- U1_1 pad 61: (no net) -> Board_1-unconnected-(U1-P1.12-Pad61)
- U1_1 pad 62: (no net) -> Board_1-unconnected-(U1-P1.13-Pad62)
- U1_1 pad 63: (no net) -> Board_1-unconnected-(U1-P1.14-Pad63)
- U1_1 pad 64: (no net) -> Board_1-unconnected-(U1-P1.15-Pad64)
- U1_1 pad 67: (no net) -> Board_1-unconnected-(U1-USB-D--Pad67)
- U1_1 pad 68: (no net) -> Board_1-unconnected-(U1-USB-D+-Pad68)
- U1_1 pad 7: (no net) -> Board_1-unconnected-(U1-P0.26-Pad7)
- U1_1 pad 8: (no net) -> Board_1-unconnected-(U1-P0.27-Pad8)
- U1_1 pad 9: (no net) -> Board_1-unconnected-(U1-P0.28-Pad9)
- U1_2 pad 1: Board_2-GND -> Board_2-/GND
- U1_2 pad 10: (no net) -> Board_2-unconnected-(U1-P0.29-Pad10)
- U1_2 pad 11: (no net) -> Board_2-unconnected-(U1-P0.30-Pad11)
- U1_2 pad 12: (no net) -> Board_2-unconnected-(U1-P0.31-Pad12)
- U1_2 pad 13: (no net) -> Board_2-unconnected-(U1-P0.00-Pad13)
- U1_2 pad 14: (no net) -> Board_2-unconnected-(U1-P0.01-Pad14)
- U1_2 pad 15: (no net) -> Board_2-unconnected-(U1-P0.02-Pad15)
- U1_2 pad 16: Board_2-GND -> Board_2-/GND
- U1_2 pad 18: Board_2-GND -> Board_2-/GND
- U1_2 pad 2: Board_2-GND -> Board_2-/GND
- U1_2 pad 20: (no net) -> Board_2-unconnected-(U1-P0.04-Pad20)
- U1_2 pad 22: (no net) -> Board_2-unconnected-(U1-P0.06-Pad22)
- U1_2 pad 24: (no net) -> Board_2-unconnected-(U1-P0.08-Pad24)
- U1_2 pad 25: (no net) -> Board_2-unconnected-(U1-P0.09-Pad25)
- U1_2 pad 26: (no net) -> Board_2-unconnected-(U1-P0.10-Pad26)
- U1_2 pad 28: (no net) -> Board_2-unconnected-(U1-P0.12-Pad28)
- U1_2 pad 29: Board_2-GND -> Board_2-/GND
- U1_2 pad 3: Board_2-GND -> Board_2-/GND
- U1_2 pad 30: Board_2-GND -> Board_2-/GND
- U1_2 pad 32: (no net) -> Board_2-unconnected-(U1-P0.14-Pad32)
- U1_2 pad 34: (no net) -> Board_2-unconnected-(U1-P0.16-Pad34)
- U1_2 pad 35: (no net) -> Board_2-unconnected-(U1-P0.17-Pad35)
- U1_2 pad 36: (no net) -> Board_2-unconnected-(U1-P0.21-Pad36)
- U1_2 pad 37: (no net) -> Board_2-unconnected-(U1-P0.19-Pad37)
- U1_2 pad 38: (no net) -> Board_2-unconnected-(U1-P0.20-Pad38)
- U1_2 pad 39: (no net) -> Board_2-unconnected-(U1-P0.18-Pad39)
- U1_2 pad 4: Board_2-GND -> Board_2-/GND
- U1_2 pad 40: (no net) -> Board_2-unconnected-(U1-P0.22-Pad40)
- U1_2 pad 41: (no net) -> Board_2-unconnected-(U1-P0.23-Pad41)
- U1_2 pad 42: (no net) -> Board_2-unconnected-(U1-P0.24-Pad42)
- U1_2 pad 45: Board_2-GND -> Board_2-/GND
- U1_2 pad 46: Board_2-GND -> Board_2-/GND
- U1_2 pad 47: Board_2-GND -> Board_2-/GND
- U1_2 pad 48: (no net) -> Board_2-unconnected-(U1-P1.05-Pad48)
- U1_2 pad 49: (no net) -> Board_2-unconnected-(U1-P1.06-Pad49)
- U1_2 pad 5: Board_2-GND -> Board_2-/GND
- U1_2 pad 50: (no net) -> Board_2-unconnected-(U1-P1.07-Pad50)
- U1_2 pad 51: (no net) -> Board_2-unconnected-(U1-P1.08-Pad51)
- U1_2 pad 52: (no net) -> Board_2-unconnected-(U1-P1.09-Pad52)
- U1_2 pad 53: (no net) -> Board_2-unconnected-(U1-P1.10-Pad53)
- U1_2 pad 54: (no net) -> Board_2-unconnected-(U1-P1.11-Pad54)
- U1_2 pad 55: Board_2-GND -> Board_2-/GND
- U1_2 pad 56: (no net) -> Board_2-unconnected-(U1-P1.00-Pad56)
- U1_2 pad 57: (no net) -> Board_2-unconnected-(U1-P1.01-Pad57)
- U1_2 pad 58: (no net) -> Board_2-unconnected-(U1-P1.02-Pad58)
- U1_2 pad 59: (no net) -> Board_2-unconnected-(U1-P1.03-Pad59)
- U1_2 pad 6: (no net) -> Board_2-unconnected-(U1-P0.25-Pad6)
- U1_2 pad 60: (no net) -> Board_2-unconnected-(U1-P1.04-Pad60)
- U1_2 pad 61: (no net) -> Board_2-unconnected-(U1-P1.12-Pad61)
- U1_2 pad 62: (no net) -> Board_2-unconnected-(U1-P1.13-Pad62)
- U1_2 pad 63: (no net) -> Board_2-unconnected-(U1-P1.14-Pad63)
- U1_2 pad 64: (no net) -> Board_2-unconnected-(U1-P1.15-Pad64)
- U1_2 pad 67: (no net) -> Board_2-unconnected-(U1-USB-D--Pad67)
- U1_2 pad 68: (no net) -> Board_2-unconnected-(U1-USB-D+-Pad68)
- U1_2 pad 7: (no net) -> Board_2-unconnected-(U1-P0.26-Pad7)
- U1_2 pad 8: (no net) -> Board_2-unconnected-(U1-P0.27-Pad8)
- U1_2 pad 9: (no net) -> Board_2-unconnected-(U1-P0.28-Pad9)
- U1_3 pad 1: Board_3-GND -> Board_3-/GND
- U1_3 pad 10: (no net) -> Board_3-unconnected-(U1-P0.29-Pad10)
- U1_3 pad 11: (no net) -> Board_3-unconnected-(U1-P0.30-Pad11)
- U1_3 pad 12: (no net) -> Board_3-unconnected-(U1-P0.31-Pad12)
- U1_3 pad 13: (no net) -> Board_3-unconnected-(U1-P0.00-Pad13)
- U1_3 pad 14: (no net) -> Board_3-unconnected-(U1-P0.01-Pad14)
- U1_3 pad 15: (no net) -> Board_3-unconnected-(U1-P0.02-Pad15)
- U1_3 pad 16: Board_3-GND -> Board_3-/GND
- U1_3 pad 18: Board_3-GND -> Board_3-/GND
- U1_3 pad 2: Board_3-GND -> Board_3-/GND
- U1_3 pad 20: (no net) -> Board_3-unconnected-(U1-P0.04-Pad20)
- U1_3 pad 22: (no net) -> Board_3-unconnected-(U1-P0.06-Pad22)
- U1_3 pad 24: (no net) -> Board_3-unconnected-(U1-P0.08-Pad24)
- U1_3 pad 25: (no net) -> Board_3-unconnected-(U1-P0.09-Pad25)
- U1_3 pad 26: (no net) -> Board_3-unconnected-(U1-P0.10-Pad26)
- U1_3 pad 28: (no net) -> Board_3-unconnected-(U1-P0.12-Pad28)
- U1_3 pad 29: Board_3-GND -> Board_3-/GND
- U1_3 pad 3: Board_3-GND -> Board_3-/GND
- U1_3 pad 30: Board_3-GND -> Board_3-/GND
- U1_3 pad 32: (no net) -> Board_3-unconnected-(U1-P0.14-Pad32)
- U1_3 pad 34: (no net) -> Board_3-unconnected-(U1-P0.16-Pad34)
- U1_3 pad 35: (no net) -> Board_3-unconnected-(U1-P0.17-Pad35)
- U1_3 pad 36: (no net) -> Board_3-unconnected-(U1-P0.21-Pad36)
- U1_3 pad 37: (no net) -> Board_3-unconnected-(U1-P0.19-Pad37)
- U1_3 pad 38: (no net) -> Board_3-unconnected-(U1-P0.20-Pad38)
- U1_3 pad 39: (no net) -> Board_3-unconnected-(U1-P0.18-Pad39)
- U1_3 pad 4: Board_3-GND -> Board_3-/GND
- U1_3 pad 40: (no net) -> Board_3-unconnected-(U1-P0.22-Pad40)
- U1_3 pad 41: (no net) -> Board_3-unconnected-(U1-P0.23-Pad41)
- U1_3 pad 42: (no net) -> Board_3-unconnected-(U1-P0.24-Pad42)
- U1_3 pad 45: Board_3-GND -> Board_3-/GND
- U1_3 pad 46: Board_3-GND -> Board_3-/GND
- U1_3 pad 47: Board_3-GND -> Board_3-/GND
- U1_3 pad 48: (no net) -> Board_3-unconnected-(U1-P1.05-Pad48)
- U1_3 pad 49: (no net) -> Board_3-unconnected-(U1-P1.06-Pad49)
- U1_3 pad 5: Board_3-GND -> Board_3-/GND
- U1_3 pad 50: (no net) -> Board_3-unconnected-(U1-P1.07-Pad50)
- U1_3 pad 51: (no net) -> Board_3-unconnected-(U1-P1.08-Pad51)
- U1_3 pad 52: (no net) -> Board_3-unconnected-(U1-P1.09-Pad52)
- U1_3 pad 53: (no net) -> Board_3-unconnected-(U1-P1.10-Pad53)
- U1_3 pad 54: (no net) -> Board_3-unconnected-(U1-P1.11-Pad54)
- U1_3 pad 55: Board_3-GND -> Board_3-/GND
- U1_3 pad 56: (no net) -> Board_3-unconnected-(U1-P1.00-Pad56)
- U1_3 pad 57: (no net) -> Board_3-unconnected-(U1-P1.01-Pad57)
- U1_3 pad 58: (no net) -> Board_3-unconnected-(U1-P1.02-Pad58)
- U1_3 pad 59: (no net) -> Board_3-unconnected-(U1-P1.03-Pad59)
- U1_3 pad 6: (no net) -> Board_3-unconnected-(U1-P0.25-Pad6)
- U1_3 pad 60: (no net) -> Board_3-unconnected-(U1-P1.04-Pad60)
- U1_3 pad 61: (no net) -> Board_3-unconnected-(U1-P1.12-Pad61)
- U1_3 pad 62: (no net) -> Board_3-unconnected-(U1-P1.13-Pad62)
- U1_3 pad 63: (no net) -> Board_3-unconnected-(U1-P1.14-Pad63)
- U1_3 pad 64: (no net) -> Board_3-unconnected-(U1-P1.15-Pad64)
- U1_3 pad 67: (no net) -> Board_3-unconnected-(U1-USB-D--Pad67)
- U1_3 pad 68: (no net) -> Board_3-unconnected-(U1-USB-D+-Pad68)
- U1_3 pad 7: (no net) -> Board_3-unconnected-(U1-P0.26-Pad7)
- U1_3 pad 8: (no net) -> Board_3-unconnected-(U1-P0.27-Pad8)
- U1_3 pad 9: (no net) -> Board_3-unconnected-(U1-P0.28-Pad9)
- U2_0 pad 1: Board_0-GND -> Board_0-/GND
- U2_0 pad 10: (no net) -> Board_0-unconnected-(U2-NC-Pad10)
- U2_0 pad 11: (no net) -> Board_0-unconnected-(U2-NC-Pad11)
- U2_0 pad 2: Board_0-GND -> Board_0-/GND
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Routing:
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- added copper zone on B.Cu, net Board_0-/GND
- added copper zone on F.Cu, net Board_0-/GND
- added copper zone on B.Cu, net Board_1-/GND
- added copper zone on F.Cu, net Board_1-/GND
- added copper zone on B.Cu, net Board_2-/GND
- added copper zone on F.Cu, net Board_2-/GND
- added copper zone on B.Cu, net Board_3-/GND
- added copper zone on F.Cu, net Board_3-/GND
- removed copper zone on B.Cu, net Board_0-GND
- removed copper zone on F.Cu, net Board_0-GND
- removed copper zone on B.Cu, net Board_1-GND
- removed copper zone on F.Cu, net Board_1-GND
- removed copper zone on B.Cu, net Board_2-GND
- removed copper zone on F.Cu, net Board_2-GND
- removed copper zone on B.Cu, net Board_3-GND
- removed copper zone on F.Cu, net Board_3-GND
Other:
- board size 91 x 88.6 mm -> 91 x 92.6 mm
- board text removed: "ShotPuck rev A"
